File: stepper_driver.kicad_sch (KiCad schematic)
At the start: 3 parts, among them U7 StepperDriver_Conn2, U8 StepperDriver, U9 StepperDriver_Conn1

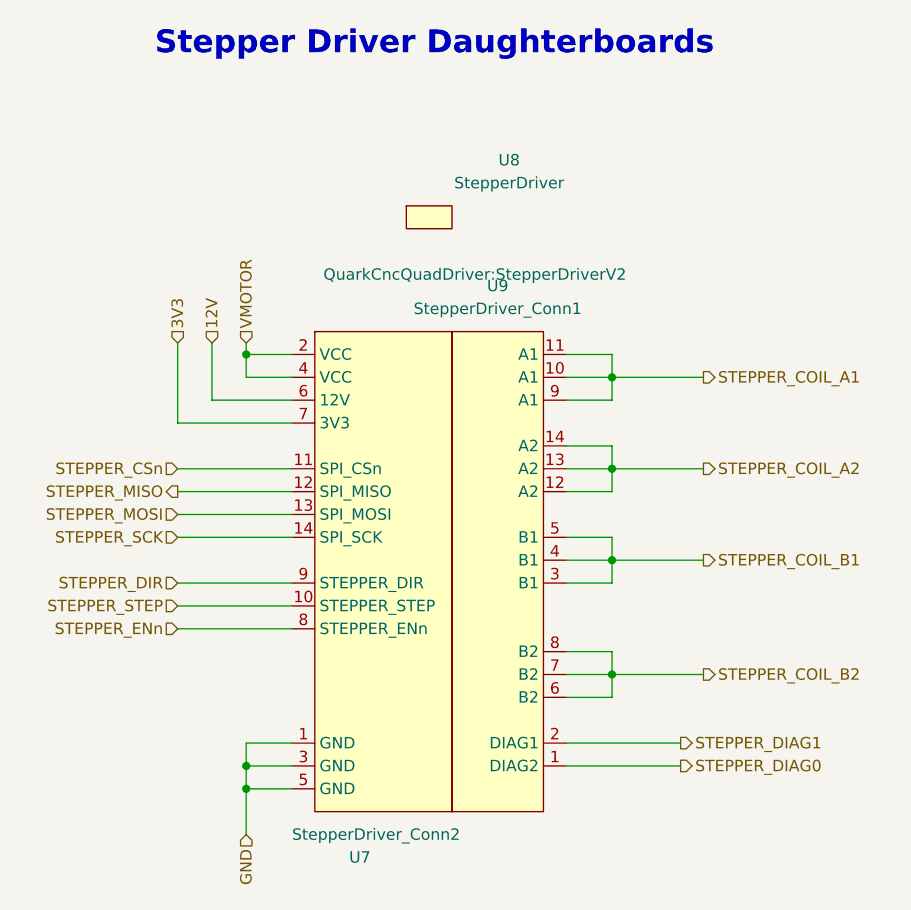
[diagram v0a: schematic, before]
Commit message: Keyed stepper drivers. Larger input connector
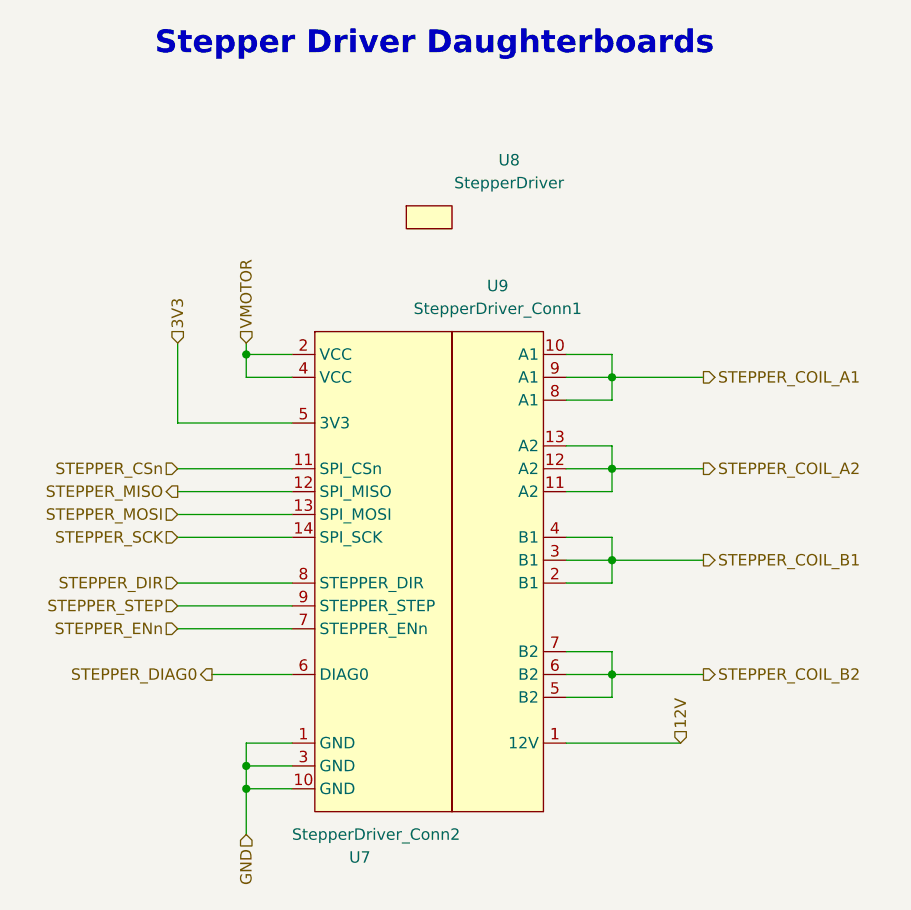
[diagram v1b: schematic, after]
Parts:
- U7: symbol QuarkCncQuadDriver:StepperDriver_Conn2_V2 -> QuarkCncQuadDriver:StepperDriver_Conn2_V3
- U8: footprint QuarkCncQuadDriver:StepperDriverV2 -> QuarkCncQuadDriver:StepperDriverV3; symbol QuarkCncQuadDriver:StepperDriver -> QuarkCncQuadDriver:StepperDriverV3
- U9: footprint Connector_PinSocket_2.54mm:PinSocket_1x14_P2.54mm_Vertical -> Connector_PinSocket_2.54mm:PinSocket_1x13_P2.54mm_Vertical; symbol QuarkCncQuadDriver:StepperDriver_Conn1 -> QuarkCncQuadDriver:StepperDriver_Conn1_V3
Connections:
- net STEPPER_DIAG1 is gone; now on net STEPPER_COIL_B1: U9.2 (B1)
- net 12V: now also U9.1 (12V); no longer U7.6 (12V)
- net 3V3: now also U7.5 (3V3); no longer U7.7 (3V3)
- net GND: now also U7.10 (GND); no longer U7.5 (GND)
- net STEPPER_COIL_A1: now also U9.8 (A1); no longer U9.11 (A1)
- net STEPPER_COIL_A2: now also U9.11 (A2); no longer U9.14 (A2)
- net STEPPER_COIL_B1: no longer U9.5 (B1)
- net STEPPER_COIL_B2: now also U9.5 (B2); no longer U9.8 (B2)
- net STEPPER_DIAG0: now also U7.6 (DIAG0); no longer U9.1 (DIAG2)
- net STEPPER_DIR: now also U7.8 (STEPPER_DIR); no longer U7.9 (STEPPER_DIR)
- net STEPPER_ENn: now also U7.7 (STEPPER_ENn); no longer U7.8 (STEPPER_ENn)
- net STEPPER_STEP: now also U7.9 (STEPPER_STEP); no longer U7.10 (STEPPER_STEP)
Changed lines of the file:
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@@
     (stroke (width 0) (type default) (color 0 0 0 0))
   )
-  (wire (pts (xy 160.02 121.92) (xy 147.32 121.92))
-    (stroke (width 0) (type solid) (color 0 0 0 0))
+  (wire (pts (xy 107.95 111.76) (xy 116.84 111.76))
+    (stroke (width 0) (type default) (color 0 0 0 0))
   )
   (wire (pts (xy 104.14 93.98) (xy 116.84 93.98))
@@
     (stroke (width 0) (type default) (color 0 0 0 0))
   )
-  (wire (pts (xy 116.84 81.28) (xy 107.95 81.28))
-    (stroke (width 0) (type default) (color 0 0 0 0))
-  )
   (wire (pts (xy 104.14 106.68) (xy 116.84 106.68))
     (stroke (width 0) (type solid) (color 0 0 0 0))
@@
   )
   (wire (pts (xy 111.76 124.46) (xy 116.84 124.46))
-    (stroke (width 0) (type default) (color 0 0 0 0))
-  )
-  (wire (pts (xy 107.95 81.28) (xy 107.95 74.93))
     (stroke (width 0) (type default) (color 0 0 0 0))
   )
@@
     (effects (font (size 1.27 1.27)) (justify left))
   )
-  (hierarchical_label "STEPPER_DIAG0" (shape output) (at 160.02 121.92 0)
-    (effects (font (size 1.27 1.27)) (justify left))
-  )
   (hierarchical_label "STEPPER_MISO" (shape output) (at 104.14 91.44 180)
     (effects (font (size 1.27 1.27)) (justify right))
@@
     (effects (font (size 1.27 1.27)) (justify right))
   )
-  (hierarchical_label "12V" (shape input) (at 107.95 74.93 90)
+  (hierarchical_label "12V" (shape input) (at 160.02 119.38 90)
     (effects (font (size 1.27 1.27)) (justify left))
   )
@@
     (effects (font (size 1.27 1.27)) (justify left))
   )
-  (hierarchical_label "STEPPER_DIAG1" (shape output) (at 160.02 119.38 0)
-    (effects (font (size 1.27 1.27)) (justify left))
+  (hierarchical_label "STEPPER_DIAG0" (shape output) (at 107.95 111.76 180)
+    (effects (font (size 1.27 1.27)) (justify right))
   )
   (hierarchical_label "STEPPER_ENn" (shape input) (at 104.14 106.68 180)
@@
     (effects (font (size 1.27 1.27)) (justify left))
   )
-  (symbol (lib_id "QuarkCncQuadDriver:StepperDriver_Conn2_V2") (at 119.38 73.66 0) (unit 1)
+  (symbol (lib_id "QuarkCncQuadDriver:StepperDriver_Conn2_V3") (at 119.38 73.66 0) (unit 1)
     (in_bom yes) (on_board yes)
     (property "Reference" "U7" (id 0) (at 123.19 132.08 0)
@@
     (pin "9")
   )
-  (symbol (lib_id "QuarkCncQuadDriver:StepperDriver") (at 129.54 59.69 0) (unit 1)
+  (symbol (lib_id "QuarkCncQuadDriver:StepperDriverV3") (at 129.54 59.69 0) (unit 1)
     (in_bom yes) (on_board yes) (fields_autoplaced)
     (property "Reference" "U8" (id 0) (at 140.97 54.61 0))
     (property "Value" "StepperDriver" (id 1) (at 140.97 57.15 0))
-    (property "Footprint" "QuarkCncQuadDriver:StepperDriverV2" (id 2) (at 137.16 67.31 0))
+    (property "Footprint" "QuarkCncQuadDriver:StepperDriverV3" (id 2) (at 137.16 67.31 0)
+      (effects (font (size 1.27 1.27)) hide)
+    )
     (property "Datasheet" "" (id 3) (at 134.62 64.77 0)
       (effects (font (size 1.27 1.27)) hide)
     )
   )
-  (symbol (lib_id "QuarkCncQuadDriver:StepperDriver_Conn1") (at 134.62 73.66 0) (unit 1)
+  (symbol (lib_id "QuarkCncQuadDriver:StepperDriver_Conn1_V3") (at 134.62 73.66 0) (unit 1)
     (in_bom yes) (on_board yes) (fields_autoplaced)
     (property "Reference" "U9" (id 0) (at 139.7 68.58 0))
     (property "Value" "StepperDriver_Conn1" (id 1) (at 139.7 71.12 0))
-    (property "Footprint" "Connector_PinSocket_2.54mm:PinSocket_1x14_P2.54mm_Vertical" (id 2) (at 149.86 66.04 0)
+    (property "Footprint" "Connector_PinSocket_2.54mm:PinSocket_1x13_P2.54mm_Vertical" (id 2) (at 149.86 66.04 0)
       (effects (font (size 1.27 1.27)) hide)
     )
@@
     (pin "12")
     (pin "13")
-    (pin "14")
     (pin "2")
     (pin "3")
